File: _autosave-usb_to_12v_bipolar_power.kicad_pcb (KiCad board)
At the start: 2 copper layers, 55.9 x 25.4 mm, 24 parts, among them J1 USB_B_Mini, J2 euro_power_header, U1 CC3-0512DF-E

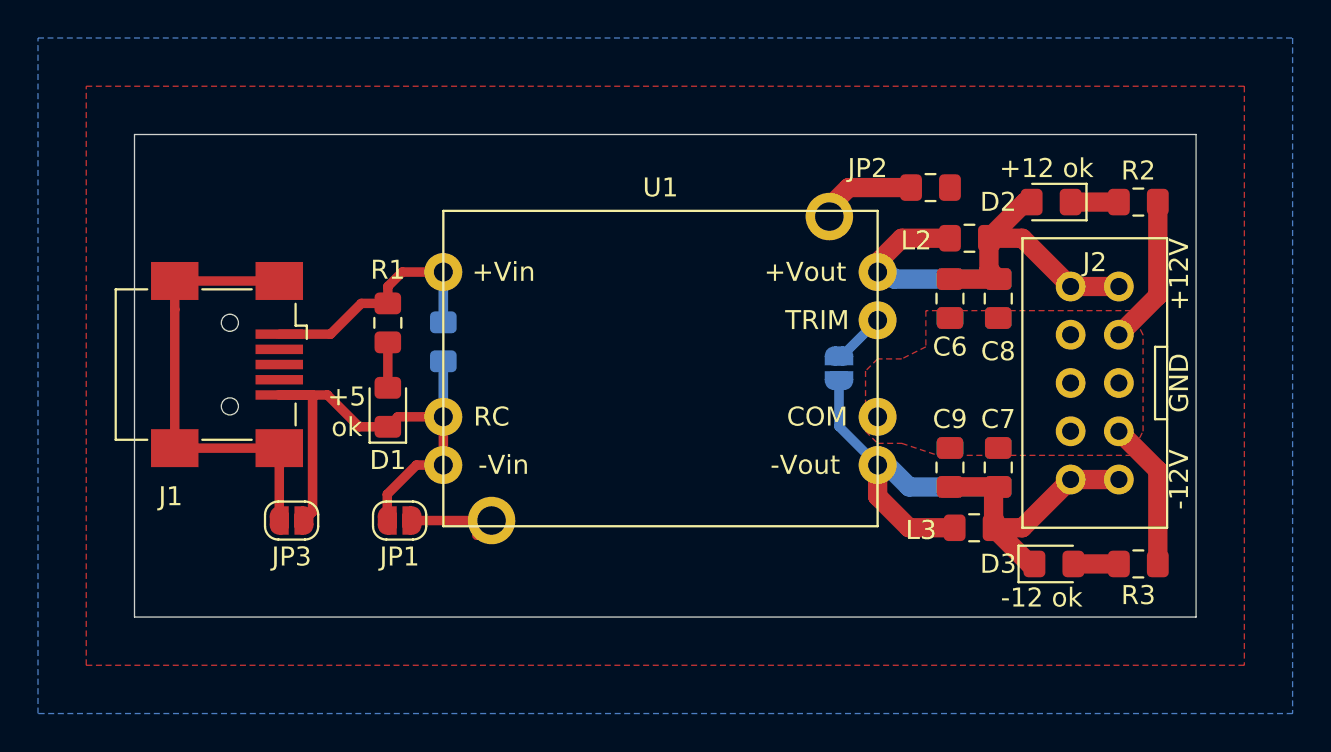
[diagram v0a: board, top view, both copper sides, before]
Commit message: change usb type, big pcb changes
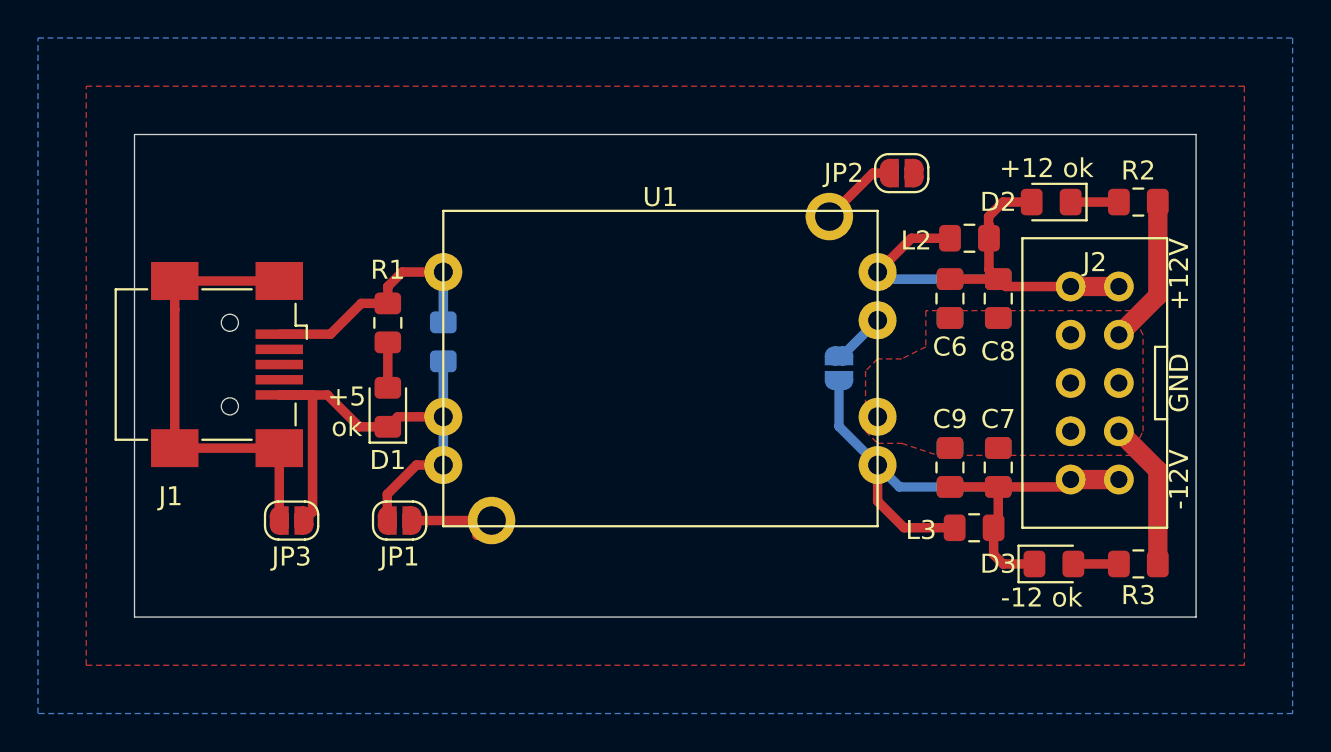
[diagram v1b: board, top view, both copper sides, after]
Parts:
- JP2: footprint Capacitor_SMD:C_0805_2012Metric_Pad1.15x1.40mm_HandSolder -> Jumper:SolderJumper-2_P1.3mm_Open_RoundedPad1.0x1.5mm
- moved JP2 1.70 mm to (147.1, 88.4)
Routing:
- net +12V: track 15.8 -> 15.1 mm
- net Net-(JP2-Pad2): track 4.72 -> 4.11 mm
- net Net-(C3-Pad2): track 19.2 -> 18.7 mm
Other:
- board text added: "+12"
- board text added: "-12"
- board text added: "gnd"
